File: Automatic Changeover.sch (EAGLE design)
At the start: 52 parts, among them IC1 ACS750LCA-050, IC2 XMEGA16A4A, IC3 XMEGA16A4A, IC4 ACS750LCA-050, IC5 ACS750LCA-050, K1 S216SE1, K2 S216SE1, K3 S216SE1, K4 S216SE1, K5 S216SE1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

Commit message: You won't believe the amount of embrassing flaws that were corrected
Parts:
- removed +OUTLET1, +OUTLET2, -OUTLET1, -OUTLET2: (no value), wirepad:3,81/1,4
- removed R2, R5, R6, R7, R8, R9: (no value), rcl:R-EU_M0805
- added DC1: (no value), dc-dc-converter:NME
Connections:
- removed net N$52: +OUTLET1.P, K3.DS1
- removed net N$54: -OUTLET2.P, K4.DS1
- removed net N$56: +OUTLET2.P, K5.DS1
- new net +OUTLET0: K3.DS1, K5.DS1
- new net -OUTLET0: K2.DS1, K4.DS1
- net +5V: now also DC1.+VIN; no longer R1.2
- net +SOURCE1: no longer -OUTLET1.P, K2.DS1
- net 3V3: now also DC1.+VOUT, R1.2
- net GND: now also DC1.-VIN, DC1.-VOUT; no longer R2.2, R5.2, R6.2
- net OUT0: no longer R2.1, R9.1, R9.2
- net OUT1: no longer R5.1, R8.1, R8.2
- net OUT2: no longer R6.1, R7.1, R7.2
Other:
- moved on the sheet: C3

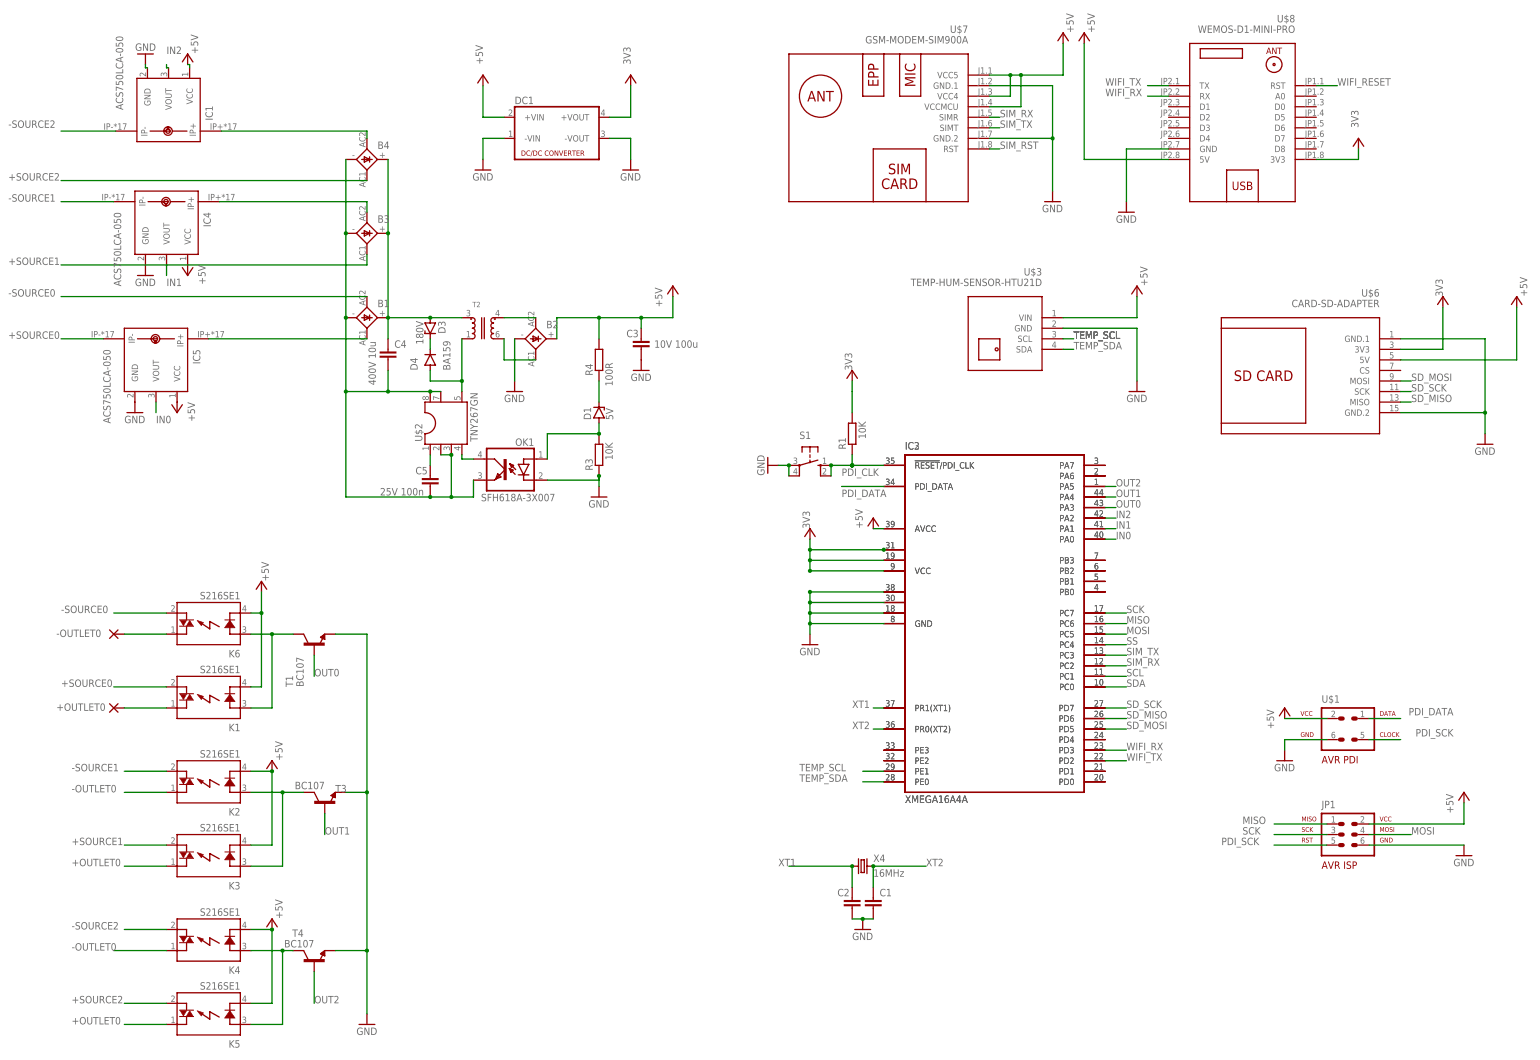
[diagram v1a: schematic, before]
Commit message: In the middle of changing the polarity of the SSR relays and also added SD_CS to MCU
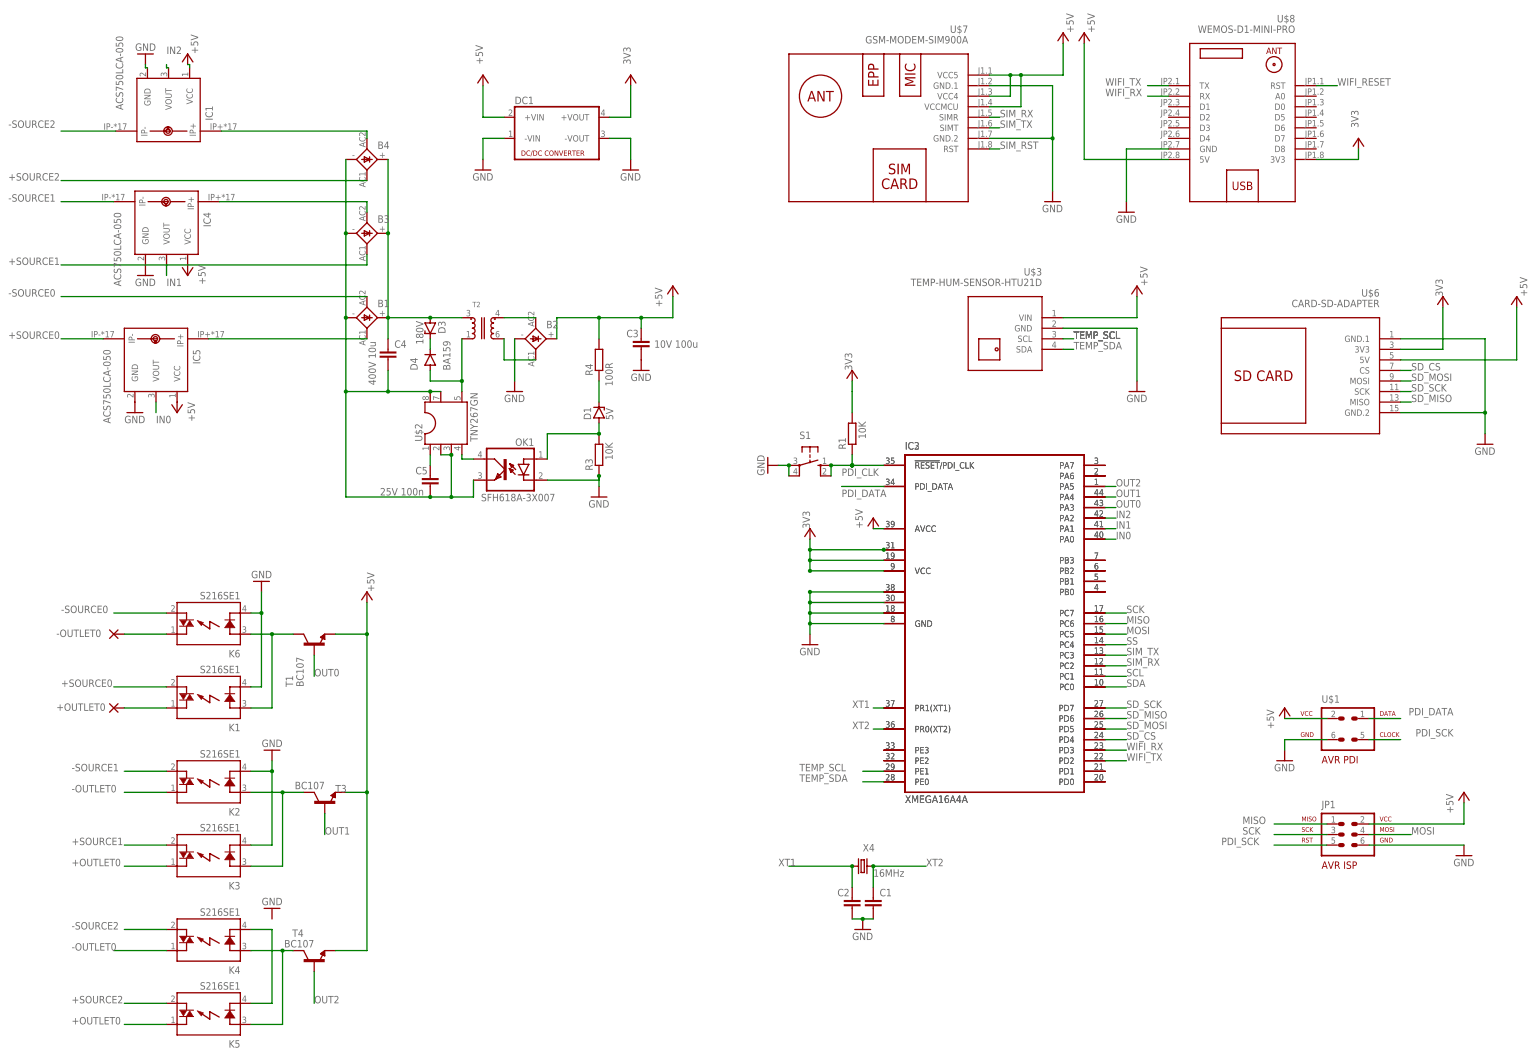
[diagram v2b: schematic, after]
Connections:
- removed net N$9: IC2.PD4, IC3.PD4
- new net N$3: K4.K, K5.K
- new net SD_CS: IC2.PD4, IC3.PD4, U$6.CS
- net +5V: now also T1.E, T3.E, T4.E; no longer K1.K, K2.K, K3.K, K4.K, K5.K, K6.K
- net GND: now also K1.K, K2.K, K3.K, K6.K; no longer T1.E, T3.E, T4.E
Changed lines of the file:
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@@
 <part name="K6" library="relay" library_urn="urn:adsk.eagle:library:339" deviceset="S2*" device="" package3d_urn="urn:adsk.eagle:package:24480/1" technology="16SE1"/>
 <part name="P+9" library="supply1" library_urn="urn:adsk.eagle:library:371" deviceset="+5V" device=""/>
-<part name="P+10" library="supply1" library_urn="urn:adsk.eagle:library:371" deviceset="+5V" device=""/>
-<part name="P+11" library="supply1" library_urn="urn:adsk.eagle:library:371" deviceset="+5V" device=""/>
 <part name="T1" library="transistor" library_urn="urn:adsk.eagle:library:402" deviceset="BC107" device="" package3d_urn="urn:adsk.eagle:package:28526/2"/>
 <part name="T3" library="transistor" library_urn="urn:adsk.eagle:library:402" deviceset="BC107" device="" package3d_urn="urn:adsk.eagle:package:28526/2"/>
@@
 <part name="GND18" library="supply1" library_urn="urn:adsk.eagle:library:371" deviceset="GND" device=""/>
 <part name="P+20" library="supply1" library_urn="urn:adsk.eagle:library:371" deviceset="VCC" device="" value="3V3"/>
+<part name="GND19" library="supply1" library_urn="urn:adsk.eagle:library:371" deviceset="GND" device=""/>
+<part name="GND20" library="supply1" library_urn="urn:adsk.eagle:library:371" deviceset="GND" device=""/>
 </parts>
 <sheets>
@@
 </instance>
 <instance part="X4" gate="G$1" x="55.88" y="-71.12" smashed="yes">
-<attribute name="NAME" x="58.42" y="-70.104" size="1.778" layer="95"/>
+<attribute name="NAME" x="55.88" y="-67.564" size="1.778" layer="95"/>
 <attribute name="VALUE" x="58.42" y="-73.66" size="1.778" layer="96"/>
 </instance>
@@
 <attribute name="VALUE" x="-93.98" y="-5.08" size="1.778" layer="96" font="vector" rot="R180"/>
 </instance>
-<instance part="P+9" gate="1" x="-88.9" y="-2.54" smashed="yes" rot="MR0">
-<attribute name="VALUE" x="-88.9" y="-2.54" size="1.778" layer="96" rot="MR90"/>
-</instance>
-<instance part="P+10" gate="1" x="-86.36" y="-45.72" smashed="yes">
-<attribute name="VALUE" x="-83.82" y="-45.72" size="1.778" layer="96" rot="R90"/>
-</instance>
-<instance part="P+11" gate="1" x="-86.36" y="-83.82" smashed="yes">
-<attribute name="VALUE" x="-83.82" y="-83.82" size="1.778" layer="96" rot="R90"/>
+<instance part="P+9" gate="1" x="-63.5" y="-5.08" smashed="yes" rot="MR0">
+<attribute name="VALUE" x="-63.5" y="-5.08" size="1.778" layer="96" rot="MR90"/>
 </instance>
 <instance part="T1" gate="G$1" x="-76.2" y="-17.78" smashed="yes" rot="R90">
@@
 <attribute name="VALUE" x="-76.2" y="-88.9" size="1.778" layer="96" rot="R180"/>
 </instance>
-<instance part="GND12" gate="1" x="-63.5" y="-109.22" smashed="yes">
-<attribute name="VALUE" x="-66.04" y="-111.76" size="1.778" layer="96"/>
+<instance part="GND12" gate="1" x="-86.36" y="-81.28" smashed="yes" rot="R180">
+<attribute name="VALUE" x="-83.82" y="-78.74" size="1.778" layer="96" rot="R180"/>
 </instance>
 <instance part="U$3" gate="G$1" x="88.9" y="55.88" smashed="yes" rot="MR0">
@@
 <instance part="P+20" gate="VCC" x="0" y="119.38" smashed="yes">
 <attribute name="VALUE" x="0" y="121.92" size="1.778" layer="96" rot="R90"/>
+</instance>
+<instance part="GND19" gate="1" x="-86.36" y="-43.18" smashed="yes" rot="R180">
+<attribute name="VALUE" x="-83.82" y="-40.64" size="1.778" layer="96" rot="R180"/>
+</instance>
+<instance part="GND20" gate="1" x="-88.9" y="-2.54" smashed="yes" rot="R180">
+<attribute name="VALUE" x="-86.36" y="0" size="1.778" layer="96" rot="R180"/>
 </instance>
 </instances>
@@
 <pinref part="IC2" gate="G$1" pin="PE3"/>
 <pinref part="IC3" gate="G$1" pin="PE3"/>
-</segment>
-</net>
-<net name="N$9" class="0">
-<segment>
-<pinref part="IC2" gate="G$1" pin="PD4"/>
-<pinref part="IC3" gate="G$1" pin="PD4"/>
 </segment>
 </net>
@@
 <wire x1="-106.68" y1="121.92" x2="-106.196571875" y2="121.92" width="0.1524" layer="91"/>
 <wire x1="-106.196571875" y1="121.92" x2="-106.196571875" y2="121.13318125" width="0.1524" layer="91"/>
-</segment>
-<segment>
-<pinref part="K1" gate="1" pin="K"/>
-<wire x1="-91.44" y1="-27.94" x2="-88.9" y2="-27.94" width="0.1524" layer="91"/>
-<wire x1="-88.9" y1="-27.94" x2="-88.9" y2="-10.16" width="0.1524" layer="91"/>
-<pinref part="P+9" gate="1" pin="+5V"/>
-<pinref part="K6" gate="1" pin="K"/>
-<wire x1="-88.9" y1="-10.16" x2="-88.9" y2="-5.08" width="0.1524" layer="91"/>
-<wire x1="-91.44" y1="-10.16" x2="-88.9" y2="-10.16" width="0.1524" layer="91"/>
-<junction x="-88.9" y="-10.16"/>
-</segment>
-<segment>
-<pinref part="K2" gate="1" pin="K"/>
-<wire x1="-91.44" y1="-48.26" x2="-86.36" y2="-48.26" width="0.1524" layer="91"/>
-<pinref part="K3" gate="1" pin="K"/>
-<wire x1="-91.44" y1="-66.04" x2="-86.36" y2="-66.04" width="0.1524" layer="91"/>
-<wire x1="-86.36" y1="-66.04" x2="-86.36" y2="-48.26" width="0.1524" layer="91"/>
-<pinref part="P+10" gate="1" pin="+5V"/>
-<junction x="-86.36" y="-48.26"/>
-</segment>
-<segment>
-<pinref part="K4" gate="1" pin="K"/>
-<wire x1="-91.44" y1="-86.36" x2="-86.36" y2="-86.36" width="0.1524" layer="91"/>
-<pinref part="K5" gate="1" pin="K"/>
-<wire x1="-91.44" y1="-104.14" x2="-86.36" y2="-104.14" width="0.1524" layer="91"/>
-<wire x1="-86.36" y1="-104.14" x2="-86.36" y2="-86.36" width="0.1524" layer="91"/>
-<pinref part="P+11" gate="1" pin="+5V"/>
-<junction x="-86.36" y="-86.36"/>
 </segment>
 <segment>
@@
 <wire x1="104.14" y1="60.96" x2="121.92" y2="60.96" width="0.1524" layer="91"/>
 <wire x1="121.92" y1="60.96" x2="121.92" y2="66.04" width="0.1524" layer="91"/>
+</segment>
+<segment>
+<pinref part="T1" gate="G$1" pin="E"/>
+<wire x1="-71.12" y1="-15.24" x2="-63.5" y2="-15.24" width="0.1524" layer="91"/>
+<wire x1="-63.5" y1="-15.24" x2="-63.5" y2="-53.34" width="0.1524" layer="91"/>
+<pinref part="T3" gate="G$1" pin="E"/>
+<wire x1="-68.58" y1="-53.34" x2="-63.5" y2="-53.34" width="0.1524" layer="91"/>
+<junction x="-63.5" y="-53.34"/>
+<pinref part="T4" gate="G$1" pin="E"/>
+<wire x1="-63.5" y1="-53.34" x2="-63.5" y2="-91.44" width="0.1524" layer="91"/>
+<wire x1="-63.5" y1="-91.44" x2="-71.12" y2="-91.44" width="0.1524" layer="91"/>
+<pinref part="P+9" gate="1" pin="+5V"/>
+<wire x1="-63.5" y1="-15.24" x2="-63.5" y2="-7.62" width="0.1524" layer="91"/>
+<junction x="-63.5" y="-15.24"/>
 </segment>
 </net>
@@
 </segment>
 <segment>
-<pinref part="T1" gate="G$1" pin="E"/>
-<wire x1="-71.12" y1="-15.24" x2="-63.5" y2="-15.24" width="0.1524" layer="91"/>
-<wire x1="-63.5" y1="-15.24" x2="-63.5" y2="-53.34" width="0.1524" layer="91"/>
-<pinref part="T3" gate="G$1" pin="E"/>
-<wire x1="-68.58" y1="-53.34" x2="-63.5" y2="-53.34" width="0.1524" layer="91"/>
-<junction x="-63.5" y="-53.34"/>
-<pinref part="T4" gate="G$1" pin="E"/>
-<wire x1="-63.5" y1="-53.34" x2="-63.5" y2="-91.44" width="0.1524" layer="91"/>
-<wire x1="-63.5" y1="-91.44" x2="-71.12" y2="-91.44" width="0.1524" layer="91"/>
-<wire x1="-63.5" y1="-91.44" x2="-63.5" y2="-106.68" width="0.1524" layer="91"/>
-<junction x="-63.5" y="-91.44"/>
-<pinref part="GND12" gate="1" pin="GND"/>
-</segment>
-<segment>
 <pinref part="U$7" gate="G$1" pin="GND.2"/>
 <pinref part="GND16" gate="1" pin="GND"/>
@@
 <pinref part="GND18" gate="1" pin="GND"/>
 <wire x1="0" y1="104.14" x2="0" y2="99.06" width="0.1524" layer="91"/>
+</segment>
+<segment>
+<pinref part="K1" gate="1" pin="K"/>
+<wire x1="-91.44" y1="-27.94" x2="-88.9" y2="-27.94" width="0.1524" layer="91"/>
+<wire x1="-88.9" y1="-27.94" x2="-88.9" y2="-10.16" width="0.1524" layer="91"/>
+<pinref part="K6" gate="1" pin="K"/>
+<wire x1="-91.44" y1="-10.16" x2="-88.9" y2="-10.16" width="0.1524" layer="91"/>
+<pinref part="GND20" gate="1" pin="GND"/>
+<wire x1="-88.9" y1="-5.08" x2="-88.9" y2="-10.16" width="0.1524" layer="91"/>
+<junction x="-88.9" y="-10.16"/>
+</segment>
+<segment>
+<pinref part="K3" gate="1" pin="K"/>
+<wire x1="-91.44" y1="-66.04" x2="-86.36" y2="-66.04" width="0.1524" layer="91"/>
+<wire x1="-86.36" y1="-66.04" x2="-86.36" y2="-48.26" width="0.1524" layer="91"/>
+<pinref part="K2" gate="1" pin="K"/>
+<wire x1="-91.44" y1="-48.26" x2="-86.36" y2="-48.26" width="0.1524" layer="91"/>
+<pinref part="GND19" gate="1" pin="GND"/>
+<wire x1="-86.36" y1="-45.72" x2="-86.36" y2="-48.26" width="0.1524" layer="91"/>
+<junction x="-86.36" y="-48.26"/>
 </segment>
 </net>
@@
 </segment>
 </net>
+<net name="SD_CS" class="0">
+<segment>
+<pinref part="U$6" gate="G$1" pin="CS"/>
+<wire x1="185.42" y1="48.26" x2="187.96" y2="48.26" width="0.1524" layer="91"/>
+<label x="187.96" y="48.26" size="1.778" layer="95"/>
+</segment>
+<segment>
+<pinref part="IC2" gate="G$1" pin="PD4"/>
+<pinref part="IC3" gate="G$1" pin="PD4"/>
+<wire x1="114.3" y1="-40.64" x2="119.38" y2="-40.64" width="0.1524" layer="91"/>
+<label x="119.38" y="-40.64" size="1.778" layer="95"/>
+</segment>
+</net>
+<net name="N$3" class="0">
+<segment>
+<pinref part="K5" gate="1" pin="K"/>
+<wire x1="-91.44" y1="-104.14" x2="-86.36" y2="-104.14" width="0.1524" layer="91"/>
+<wire x1="-86.36" y1="-104.14" x2="-86.36" y2="-86.36" width="0.1524" layer="91"/>
+<pinref part="K4" gate="1" pin="K"/>
+<wire x1="-91.44" y1="-86.36" x2="-86.36" y2="-86.36" width="0.1524" layer="91"/>
+</segment>
+</net>
